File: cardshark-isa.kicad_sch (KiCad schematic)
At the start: 99 parts, among them J1 Conn_02x13_Odd_Even, J3 DE15_Receptacle_HighDensity_M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, J4 Bus_ISA_16bit, U1 GD543x_ISA, U11 93CxxA, U12 SOJ_256Kx16, U13 SOJ_256Kx16, U2 27C256, U3 SOJ_256Kx16, U5 74AHCT1G04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

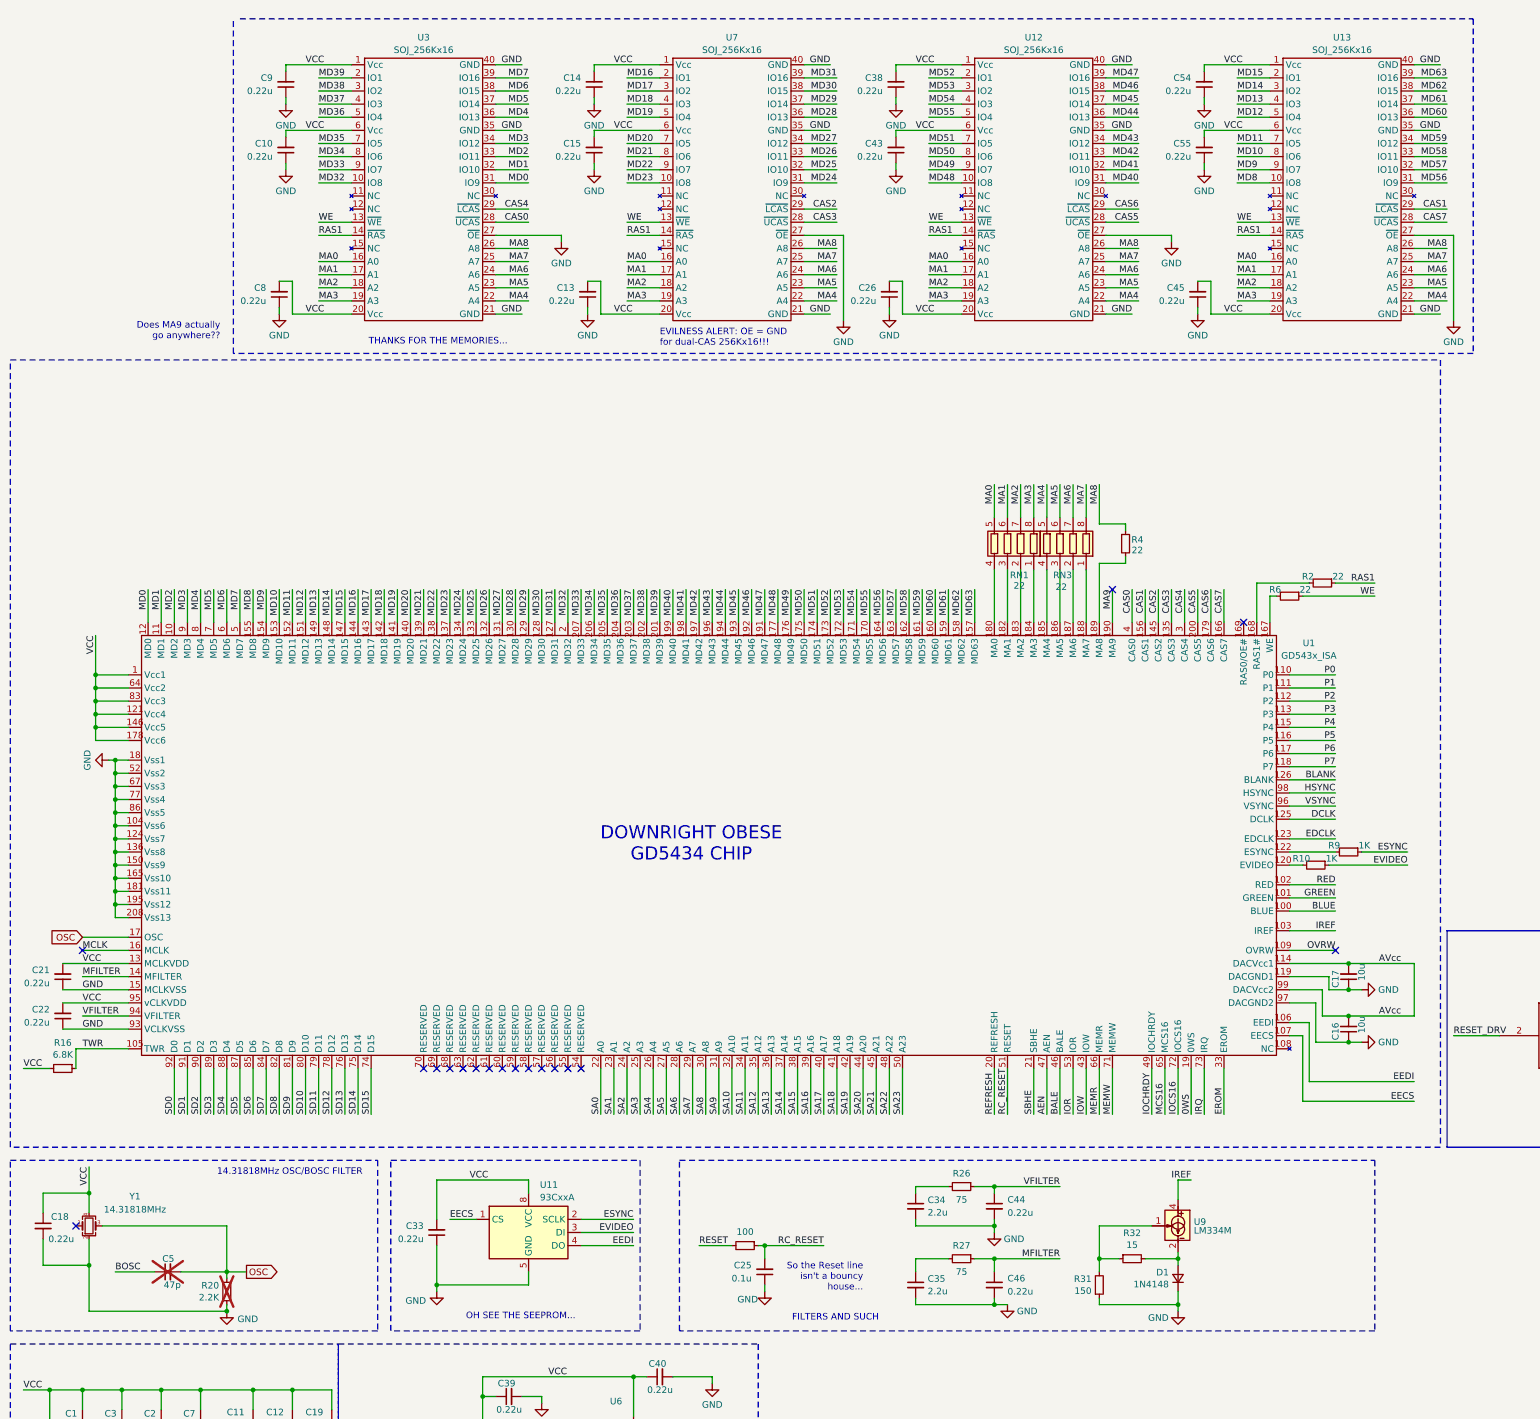
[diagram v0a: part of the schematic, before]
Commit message: Add files via upload
Uploaded wrong version of board files by mistake; uploaded correct working version this time
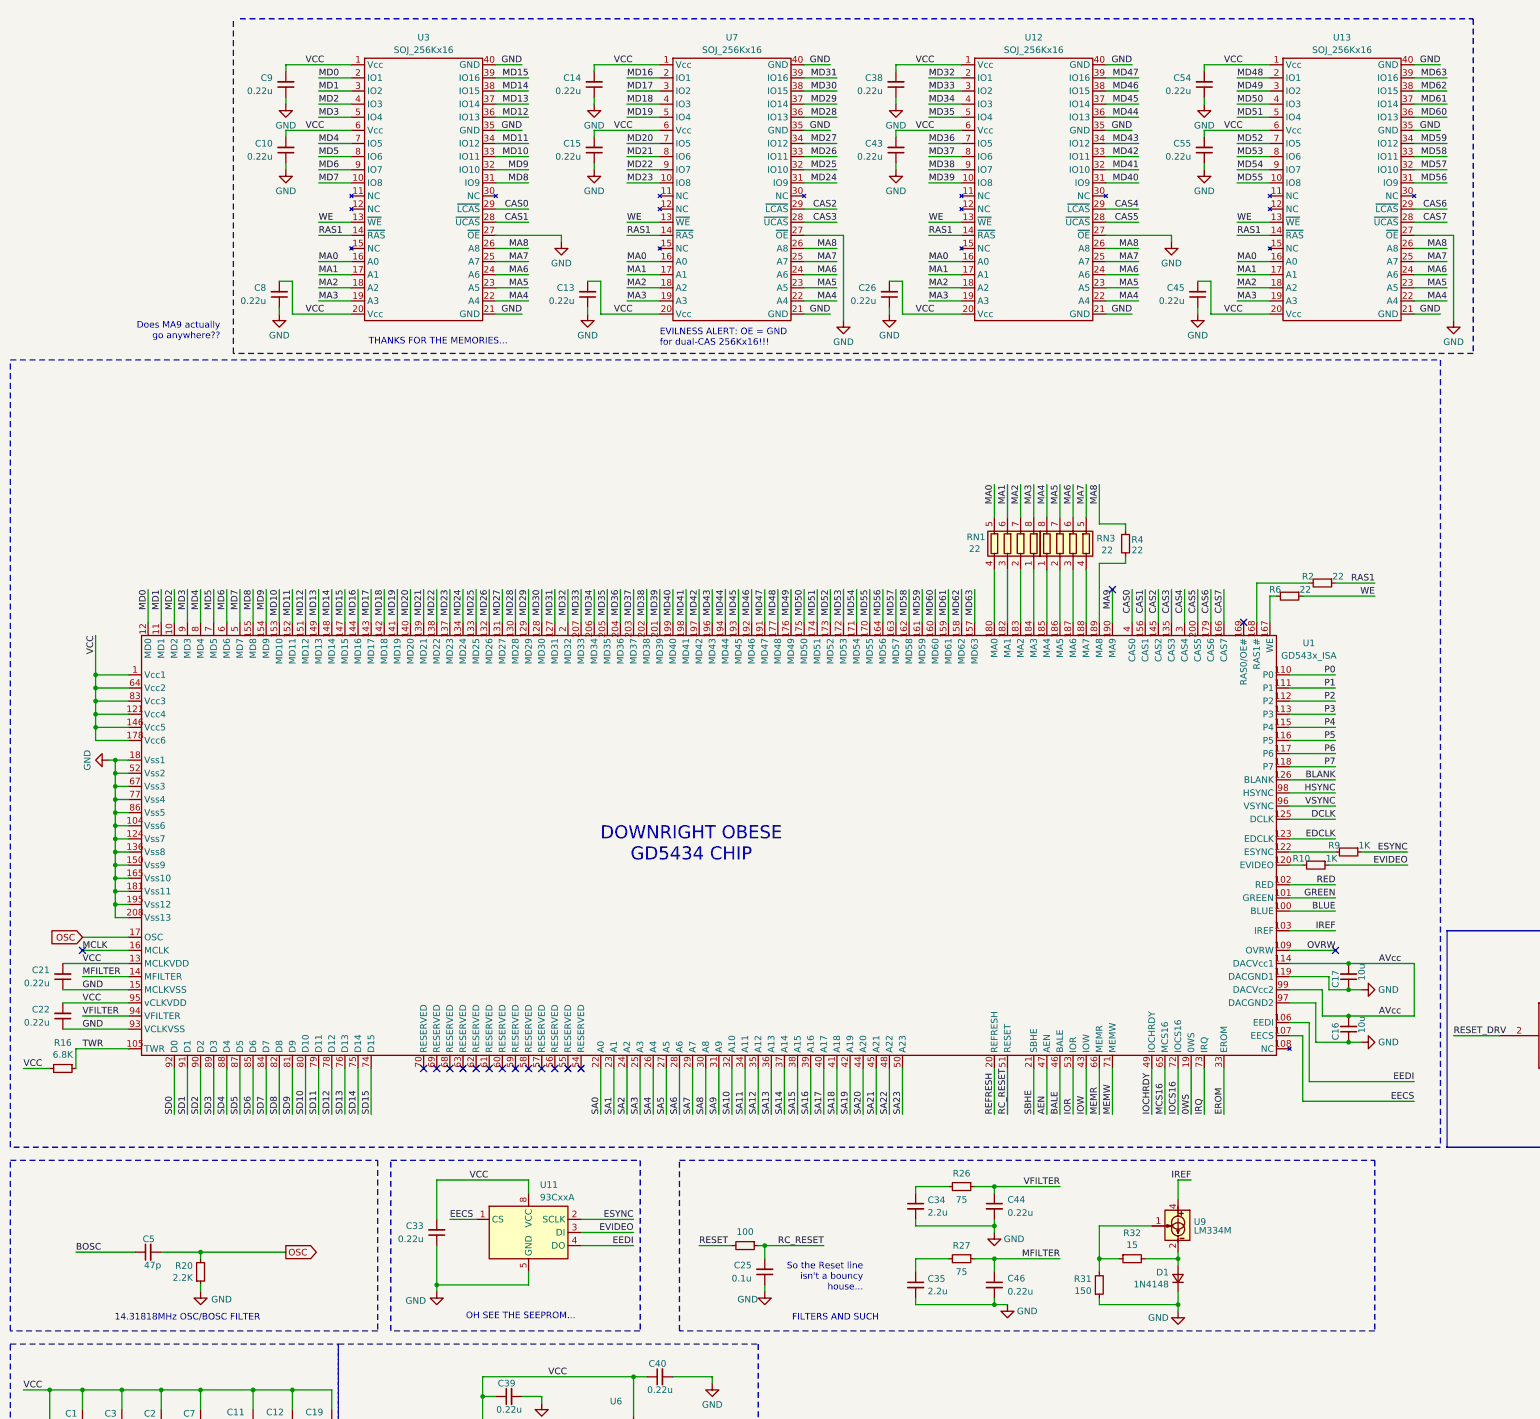
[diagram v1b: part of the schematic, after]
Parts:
- removed C18: 0.22u, Capacitor_SMD:C_0805_2012Metric, symbol Device:C_Small
- removed Y1: 14.31818MHz, Crystal:Crystal_SMD_7050-4Pin_7.0x5.0mm, symbol Device:Crystal_GND24_Small
- C5, R20: now fitted
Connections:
- net CAS0: now also U3.29 (~{LCAS}); no longer U3.28 (~{UCAS})
- net CAS1: now also U3.28 (~{UCAS}); no longer U13.29 (~{LCAS})
- net CAS4: now also U12.29 (~{LCAS}); no longer U3.29 (~{LCAS})
- net CAS6: now also U13.29 (~{LCAS}); no longer U12.29 (~{LCAS})
- net MA4: now also RN3.8 (R1.2); no longer RN3.5 (R4.2)
- net MA5: now also RN3.7 (R2.2); no longer RN3.6 (R3.2)
- net MA6: now also RN3.6 (R3.2); no longer RN3.7 (R2.2)
- net MA7: now also RN3.5 (R4.2); no longer RN3.8 (R1.2)
- net MD0: now also U3.2 (IO1); no longer U3.31 (IO9)
- net MD1: now also U3.3 (IO2); no longer U3.32 (IO10)
- net MD10: now also U3.33 (IO11); no longer U13.8 (IO6)
- net MD11: now also U3.34 (IO12); no longer U13.7 (IO5)
- net MD12: now also U3.36 (IO13); no longer U13.5 (IO4)
- net MD13: now also U3.37 (IO14); no longer U13.4 (IO3)
- net MD14: now also U3.38 (IO15); no longer U13.3 (IO2)
- net MD15: now also U3.39 (IO16); no longer U13.2 (IO1)
- net MD2: now also U3.4 (IO3); no longer U3.33 (IO11)
- net MD3: now also U3.5 (IO4); no longer U3.34 (IO12)
- net MD32: now also U12.2 (IO1); no longer U3.10 (IO8)
- net MD33: now also U12.3 (IO2); no longer U3.9 (IO7)
- net MD34: now also U12.4 (IO3); no longer U3.8 (IO6)
- net MD35: now also U12.5 (IO4); no longer U3.7 (IO5)
- net MD36: now also U12.7 (IO5); no longer U3.5 (IO4)
- net MD37: now also U12.8 (IO6); no longer U3.4 (IO3)
- net MD38: now also U12.9 (IO7); no longer U3.3 (IO2)
- net MD39: now also U12.10 (IO8); no longer U3.2 (IO1)
- net MD4: now also U3.7 (IO5); no longer U3.36 (IO13)
- net MD48: now also U13.2 (IO1); no longer U12.10 (IO8)
- net MD49: now also U13.3 (IO2); no longer U12.9 (IO7)
- net MD5: now also U3.8 (IO6); no longer U3.37 (IO14)
- net MD50: now also U13.4 (IO3); no longer U12.8 (IO6)
- net MD51: now also U13.5 (IO4); no longer U12.7 (IO5)
- net MD52: now also U13.7 (IO5); no longer U12.2 (IO1)
- net MD53: now also U13.8 (IO6); no longer U12.3 (IO2)
- net MD54: now also U13.9 (IO7); no longer U12.4 (IO3)
- net MD55: now also U13.10 (IO8); no longer U12.5 (IO4)
- net MD6: now also U3.9 (IO7); no longer U3.38 (IO15)
- net MD7: now also U3.10 (IO8); no longer U3.39 (IO16)
- net MD8: now also U3.31 (IO9); no longer U13.10 (IO8)
- net MD9: now also U3.32 (IO10); no longer U13.9 (IO7)
- net at RN3.1 (R1.1): now also U1.185 (MA4); no longer U1.188 (MA7)
- net at RN3.2 (R2.1): now also U1.186 (MA5); no longer U1.187 (MA6)
- net at RN3.3 (R3.1): now also U1.187 (MA6); no longer U1.186 (MA5)
- net at RN3.4 (R4.1): now also U1.188 (MA7); no longer U1.185 (MA4)
- no-connect marks 58 -> 57
